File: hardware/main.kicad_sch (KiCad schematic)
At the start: 15 parts, among them J3 Conn_01x01_Pin, J4 Conn_01x01_Pin, J5 Conn_01x01_Pin, J6 Conn_01x01_Pin, K2 ADW11

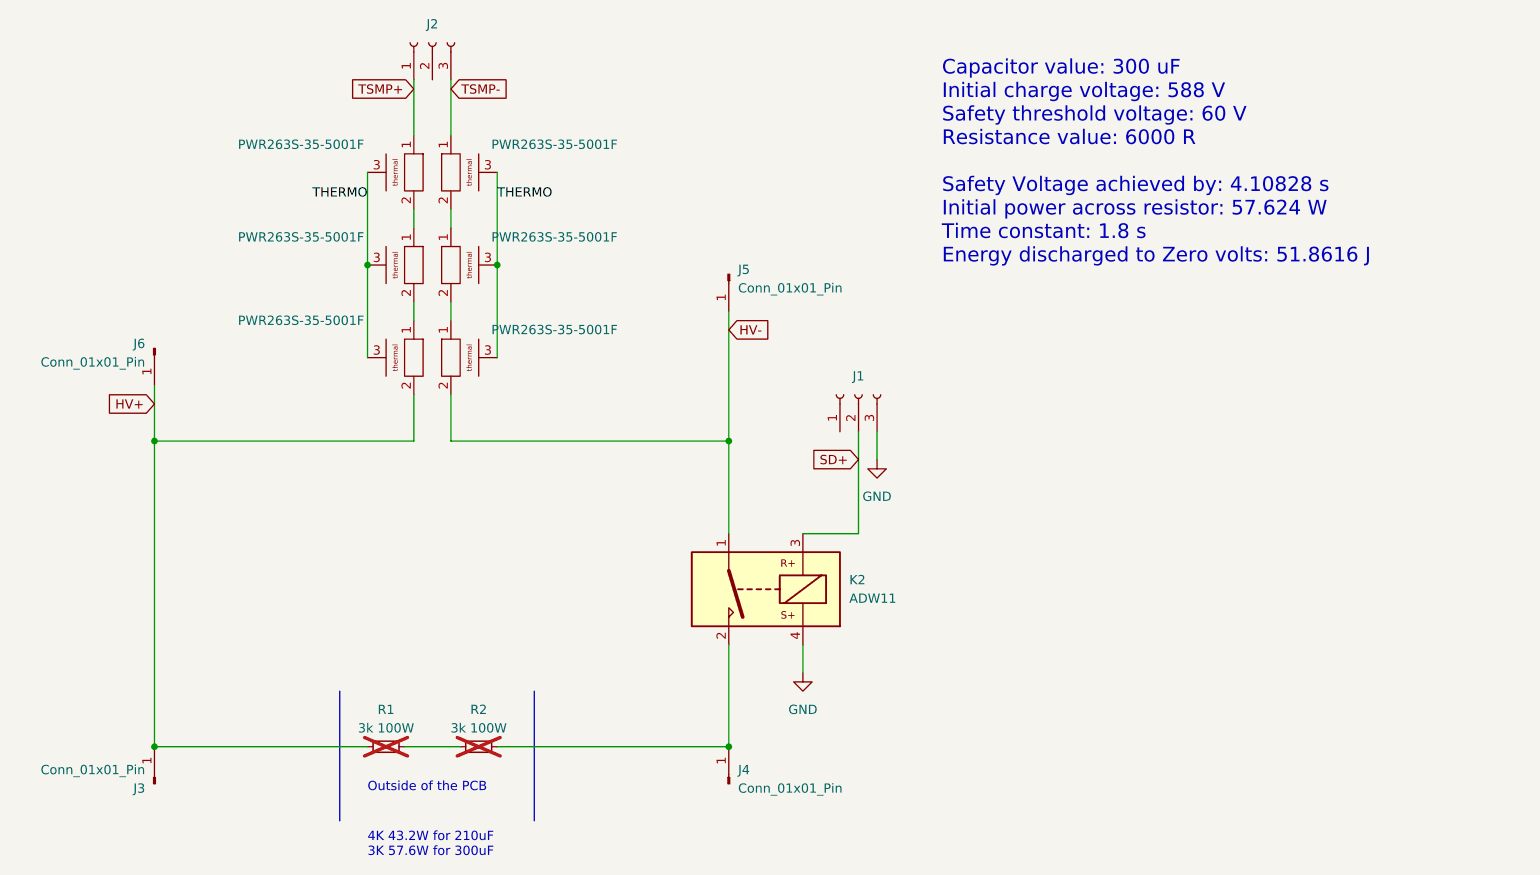
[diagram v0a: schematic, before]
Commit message: updated layout with connections
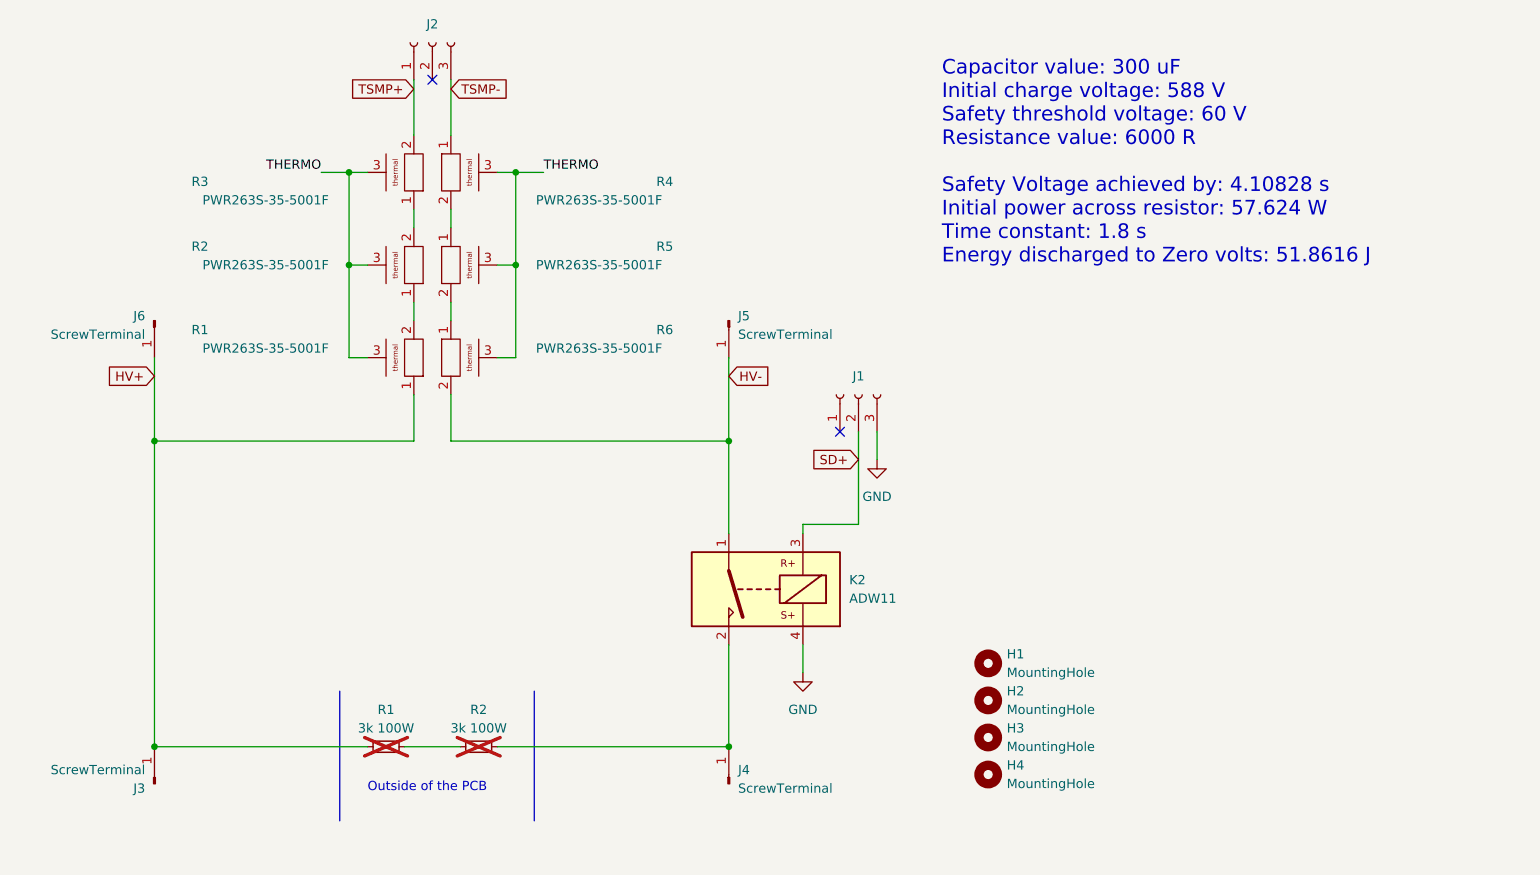
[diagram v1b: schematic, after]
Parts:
- added H1, H2, H3, H4: MountingHole, MountingHole:MountingHole_3.2mm_M3, symbol Mechanical:MountingHole
- J3, J4, J5, J6: value Conn_01x01_Pin -> ScrewTerminal
- R1, R2, R3, R4, R5, R6: renamed from PWR263S-35-5001F; value ~ -> PWR263S-35-5001F; footprint (none) -> 7696:PWR263S-35-5001F
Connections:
- net HV+: now also R1.1; no longer R3.2
- net TSMP+: now also R3.2; no longer R1.1
- no-connect marks 0 -> 2
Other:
- note removed: "4K 43.2W for 210uF 3K 57.6W for 300uF"
- moved on the sheet: J5, J6, R1, R2, R3

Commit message: Fabrication Toolkit files added
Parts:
- removed J3: ScrewTerminal, 7696:7696, symbol Connector:Conn_01x01_Pin
- R1, R2: now fitted
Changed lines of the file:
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@@
   (junction (at 85.09 52.07) (diameter 0) (color 0 0 0 0)
-  )
-  (junction (at 35.56 130.81) (diameter 0) (color 0 0 0 0)
   )
   (junction (at 62.23 64.77) (diameter 0) (color 0 0 0 0)
@@
   )
   (symbol (lib_id "Device:R_Small") (at 80.01 130.81 90) (unit 1)
-    (in_bom no) (on_board no) (dnp yes) (fields_autoplaced)
+    (in_bom no) (on_board no) (dnp no) (fields_autoplaced)
     (property "Reference" "R2" (at 80.01 125.73 90)
       (effects (font (size 1.27 1.27)))
@@
     )
   )
-  (symbol (lib_id "Connector:Conn_01x01_Pin") (at 35.56 135.89 90) (unit 1)
-    (in_bom yes) (on_board yes) (dnp no)
-    (property "Reference" "J3" (at 34.29 136.525 90)
-      (effects (font (size 1.27 1.27)) (justify left))
-    )
-    (property "Value" "ScrewTerminal" (at 34.29 133.985 90)
-      (effects (font (size 1.27 1.27)) (justify left))
-    )
-    (property "Footprint" "7696:7696" (at 35.56 135.89 0)
-      (effects (font (size 1.27 1.27)) hide)
-    )
-    (property "Datasheet" "~" (at 35.56 135.89 0)
-      (effects (font (size 1.27 1.27)) hide)
-    )
-    (pin "1")
-    (instances
-      (project "main"
-        (path "/b652b05a-4e3d-4ad1-b032-18886abe7d45"
-          (reference "J3") (unit 1)
-        )
-      )
-    )
-  )
   (symbol (lib_id "power:GND") (at 134.62 91.44 0) (unit 1)
     (in_bom yes) (on_board yes) (dnp no) (fields_autoplaced)
@@
   )
   (symbol (lib_id "Device:R_Small") (at 67.31 130.81 90) (unit 1)
-    (in_bom no) (on_board no) (dnp yes) (fields_autoplaced)
+    (in_bom no) (on_board no) (dnp no) (fields_autoplaced)
     (property "Reference" "R1" (at 67.31 125.73 90)
       (effects (font (size 1.27 1.27)))
